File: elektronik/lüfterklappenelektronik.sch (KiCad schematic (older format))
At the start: 33 parts

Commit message: avr utils framework
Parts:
- R? (x3): value 50 -> 120
- R? (x3): value 20K -> 2K2
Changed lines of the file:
@@
 LIBS:contrib
 LIBS:valves
+LIBS:lüfterklappenelektronik-cache
 EELAYER 25 0
 EELAYER END
@@
 P 1150 1200
 F 0 "R?" H 1220 1246 50  0000 L CNN
-F 1 "50" H 1220 1155 50  0000 L CNN
+F 1 "120" H 1220 1155 50  0000 L CNN
 F 2 "" V 1080 1200 50  0000 C CNN
 F 3 "" H 1150 1200 50  0000 C CNN
@@
 P 2350 2050
 F 0 "R?" H 2420 2096 50  0000 L CNN
-F 1 "20K" H 2420 2005 50  0000 L CNN
+F 1 "2K2" H 2420 2005 50  0000 L CNN
 F 2 "" V 2280 2050 50  0000 C CNN
 F 3 "" H 2350 2050 50  0000 C CNN
@@
 P 1150 2950
 F 0 "R?" H 1220 2996 50  0000 L CNN
-F 1 "50" H 1220 2905 50  0000 L CNN
+F 1 "120" H 1220 2905 50  0000 L CNN
 F 2 "" V 1080 2950 50  0000 C CNN
 F 3 "" H 1150 2950 50  0000 C CNN
@@
 P 2350 3800
 F 0 "R?" H 2420 3846 50  0000 L CNN
-F 1 "20K" H 2420 3755 50  0000 L CNN
+F 1 "2K2" H 2420 3755 50  0000 L CNN
 F 2 "" V 2280 3800 50  0000 C CNN
 F 3 "" H 2350 3800 50  0000 C CNN
@@
 P 1150 4600
 F 0 "R?" H 1220 4646 50  0000 L CNN
-F 1 "50" H 1220 4555 50  0000 L CNN
+F 1 "120" H 1220 4555 50  0000 L CNN
 F 2 "" V 1080 4600 50  0000 C CNN
 F 3 "" H 1150 4600 50  0000 C CNN
@@
 P 2350 5450
 F 0 "R?" H 2420 5496 50  0000 L CNN
-F 1 "20K" H 2420 5405 50  0000 L CNN
+F 1 "2K2" H 2420 5405 50  0000 L CNN
 F 2 "" V 2280 5450 50  0000 C CNN
 F 3 "" H 2350 5450 50  0000 C CNN

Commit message: lot's of debugging makes things work
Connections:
- wire segments 56 -> 57
- no-connect marks 1 -> 0
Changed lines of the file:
@@
 Text Label 6750 2000 2    60   ~ 0
 PS1SS
-NoConn ~ 6450 2000
 $Comp
 L CONN_01X04 P?
@@
 Connection ~ 6550 2100
 Connection ~ 6550 1600
+Text Label 6450 2400 0    60   ~ 0
+EndstopDamper1
 Text Label 6450 2500 0    60   ~ 0
-EndstopDamper1
+EndstopDamper2
 Text Label 6450 2600 0    60   ~ 0
-EndstopDamper2
-Text Label 6450 2700 0    60   ~ 0
 EndstopDamper3
-Text Label 6450 4400 0    60   ~ 0
+Text Label 6450 3800 0    60   ~ 0
 FAN
 Text Label 6450 3400 0    60   ~ 0
@@
 Text Label 4700 800  2    60   ~ 0
 PJON
+Text Label 6450 3500 0    60   ~ 0
+PJON
+Wire Wire Line
+	6450 2000 6750 2000
+Text Label 6450 2700 0    60   ~ 0
+PS2SS
+Text Label 6450 2900 0    60   ~ 0
+PS3SS
 $EndSCHEMATC

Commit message: notes and todo
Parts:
- C?: value C -> C_SSR
- P?: value FAN_Phase -> FAN_230VAC_Phase
- R?: value R -> R_SSR
- R? (x4): value R -> 100
- U?: value S102S02 -> ZG3NC-240B
- VR?: value VR -> S7K275
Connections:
- wire segments 57 -> 58
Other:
- note added: "SSR LED pulls <=19mA per test and 40mA per datasheet\nWe _could_probably connect it directly to the Teensy via 12 Ohm R\nor maybe 47Ohm R which means 2V drop on 40mA and 0.5V drop\non 10mA so we may naturally limit the current.\nRelay LED minimum Voltage is 3V"
- moved on the sheet: P?, VR?
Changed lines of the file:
@@
 L VR VR?
 U 1 1 5741999A
-P 5750 6650
-F 0 "VR?" H 5838 6696 50  0000 L CNN
-F 1 "VR" H 5838 6605 50  0000 L CNN
-F 2 "" H 5750 6650 50  0000 C CNN
-F 3 "" H 5750 6650 50  0000 C CNN
-	1    5750 6650
+P 5850 6700
+F 0 "VR?" H 5938 6746 50  0000 L CNN
+F 1 "S7K275" H 5938 6655 50  0000 L CNN
+F 2 "" H 5850 6700 50  0000 C CNN
+F 3 "" H 5850 6700 50  0000 C CNN
+	1    5850 6700
 	1    0    0    -1
 $EndComp
@@
 P 4900 6500
 F 0 "U?" H 4900 6915 50  0000 C CNN
-F 1 "S102S02" H 4900 6824 50  0000 C CNN
+F 1 "ZG3NC-240B" H 4900 6824 50  0000 C CNN
 F 2 "SIP4_Sharp-SSR" H 4900 6733 50  0000 C CIN
 F 3 "" H 4865 6500 50  0000 L CNN
@@
 P 5450 6550
 F 0 "R?" H 5520 6596 50  0000 L CNN
-F 1 "R" H 5520 6505 50  0000 L CNN
+F 1 "R_SSR" H 5520 6505 50  0000 L CNN
 F 2 "" V 5380 6550 50  0000 C CNN
 F 3 "" H 5450 6550 50  0000 C CNN
@@
 P 5450 6850
 F 0 "C?" H 5565 6896 50  0000 L CNN
-F 1 "C" H 5565 6805 50  0000 L CNN
+F 1 "C_SSR" H 5565 6805 50  0000 L CNN
 F 2 "" H 5488 6700 50  0000 C CNN
 F 3 "" H 5450 6850 50  0000 C CNN
@@
 P 8650 1900
 F 0 "R?" V 8443 1900 50  0000 C CNN
-F 1 "R" V 8534 1900 50  0000 C CNN
+F 1 "100" V 8534 1900 50  0000 C CNN
 F 2 "" V 8580 1900 50  0000 C CNN
 F 3 "" H 8650 1900 50  0000 C CNN
@@
 P 8650 3550
 F 0 "R?" V 8443 3550 50  0000 C CNN
-F 1 "R" V 8534 3550 50  0000 C CNN
+F 1 "100" V 8534 3550 50  0000 C CNN
 F 2 "" V 8580 3550 50  0000 C CNN
 F 3 "" H 8650 3550 50  0000 C CNN
@@
 P 8650 5200
 F 0 "R?" V 8443 5200 50  0000 C CNN
-F 1 "R" V 8534 5200 50  0000 C CNN
+F 1 "100" V 8534 5200 50  0000 C CNN
 F 2 "" V 8580 5200 50  0000 C CNN
 F 3 "" H 8650 5200 50  0000 C CNN
@@
 P 4050 6950
 F 0 "R?" V 3843 6950 50  0000 C CNN
-F 1 "R" V 3934 6950 50  0000 C CNN
+F 1 "100" V 3934 6950 50  0000 C CNN
 F 2 "" V 3980 6950 50  0000 C CNN
 F 3 "" H 4050 6950 50  0000 C CNN
@@
 	3800 6950 3900 6950
 Wire Wire Line
-	5200 6400 6050 6400
+	5200 6400 6200 6400
 Connection ~ 5450 6400
-Wire Wire Line
-	5200 7000 6050 7000
-Wire Wire Line
-	5750 7000 5750 6900
 Wire Wire Line
 	5200 7000 5200 6600
@@
 L CONN_01X02 P?
 U 1 1 5741BBF0
-P 6250 6450
-F 0 "P?" H 6327 6491 50  0000 L CNN
-F 1 "FAN_Phase" H 6327 6400 50  0000 L CNN
-F 2 "" H 6250 6450 50  0000 C CNN
-F 3 "" H 6250 6450 50  0000 C CNN
-	1    6250 6450
-	1    0    0    -1
-$EndComp
-Connection ~ 5750 6400
-Wire Wire Line
-	6050 7000 6050 6500
-Connection ~ 5750 7000
+P 6400 6450
+F 0 "P?" H 6477 6491 50  0000 L CNN
+F 1 "FAN_230VAC_Phase" H 6477 6400 50  0000 L CNN
+F 2 "" H 6400 6450 50  0000 C CNN
+F 3 "" H 6400 6450 50  0000 C CNN
+	1    6400 6450
+	1    0    0    -1
+$EndComp
 $Comp
 L PHOTORESISTOR U?
@@
 Text Label 6450 2900 0    60   ~ 0
 PS3SS
+Text Notes 1400 7550 0    60   ~ 0
+SSR LED pulls <=19mA per test and 40mA per datasheet\nWe _could_probably connect it directly to the Teensy via 12 Ohm R\nor maybe 47Ohm R which means 2V drop on 40mA and 0.5V drop\non 10mA so we may naturally limit the current.\nRelay LED minimum Voltage is 3V
+Wire Wire Line
+	5850 6450 5850 6400
+Connection ~ 5850 6400
+Wire Wire Line
+	5200 7000 6200 7000
+Wire Wire Line
+	6200 7000 6200 6500
+Wire Wire Line
+	5850 6950 5850 7000
+Connection ~ 5850 7000
 $EndSCHEMATC

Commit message: update
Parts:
- removed P?: CONN_PJON, symbol CONN_01X02
- removed Q?: BC413, TO-92, symbol BC413
- added P101: CONN_01X04, symbol CONN_01X04
- gave numbers to parts that had none: 31
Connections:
- wire segments 58 -> 61
- no-connect marks 0 -> 24
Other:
- note removed: "SSR LED pulls <=19mA per test and 40mA per datasheet\nWe _could_probably connect it directly to the Teensy via 12 Ohm R\nor maybe 47Ohm R which means 2V drop on 40mA and 0.5V drop\non 10mA so we may naturally limit the current.\nRelay LED minimum Voltage is 3V"

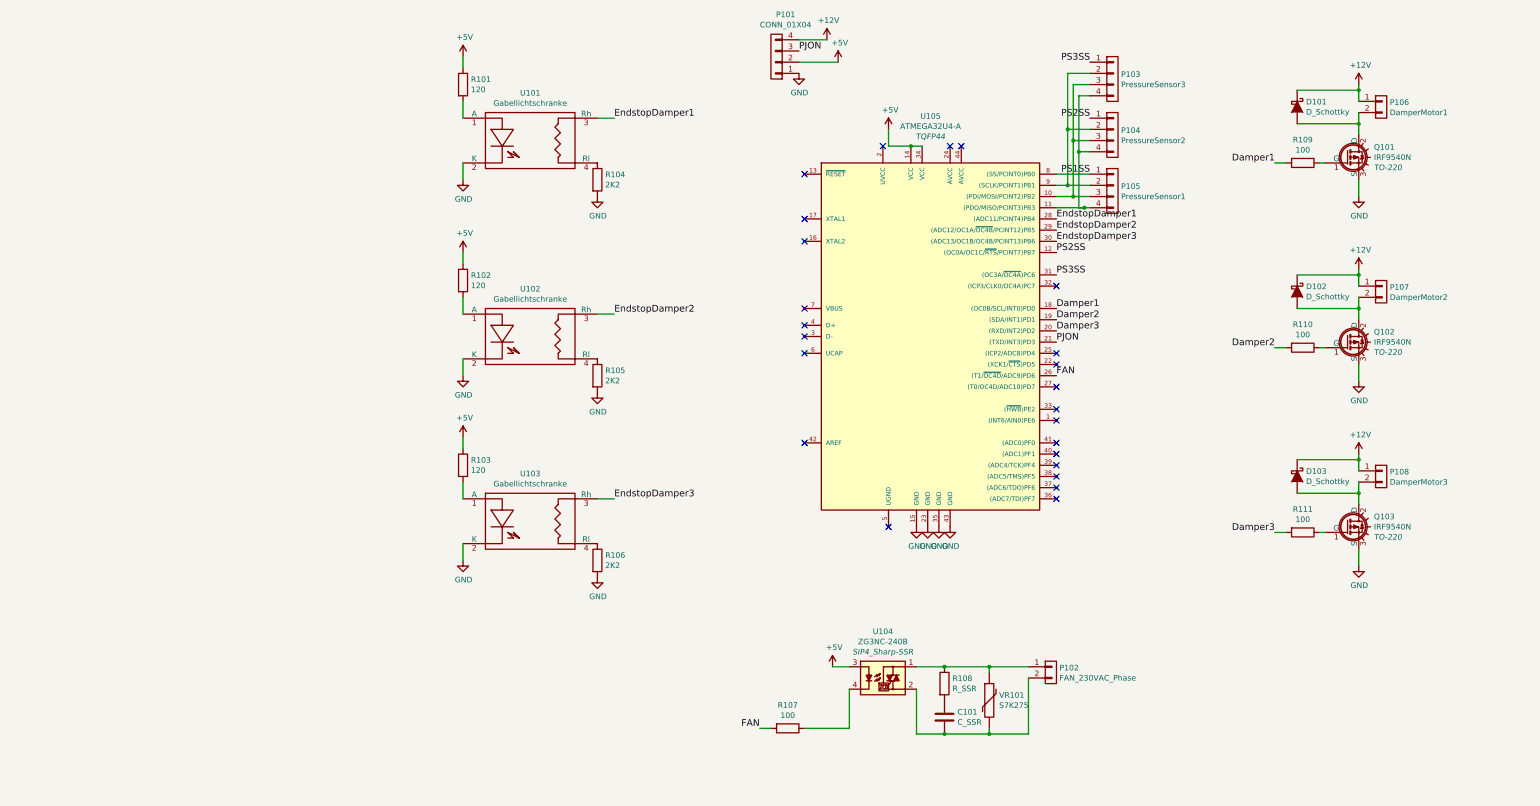
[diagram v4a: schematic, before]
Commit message: pin changes for arduinoProMicro
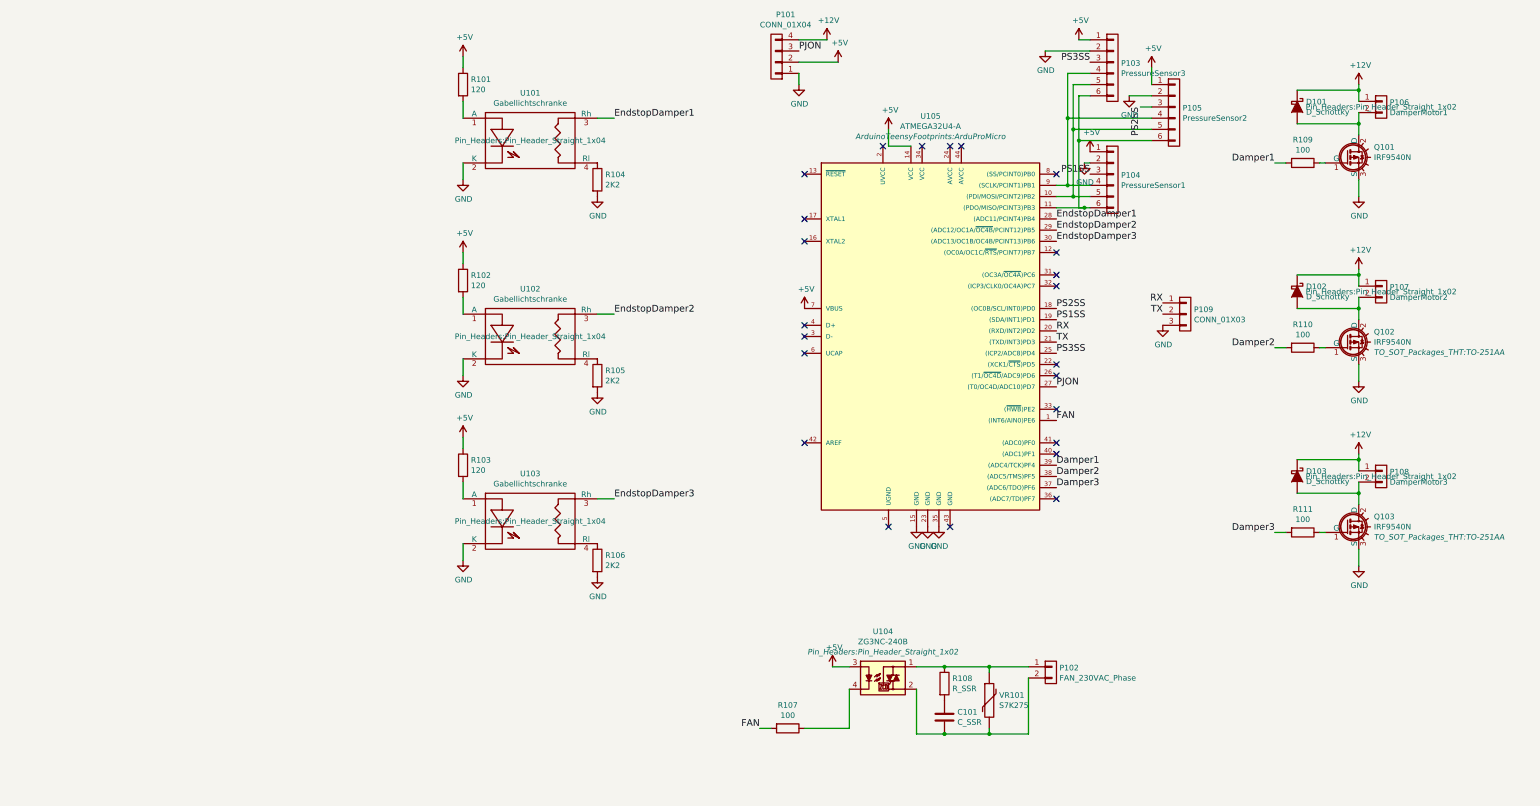
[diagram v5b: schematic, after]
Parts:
- removed P103: PressureSensor3, symbol CONN_01X04
- removed P104: PressureSensor2, symbol CONN_01X04
- removed P105: PressureSensor1, symbol CONN_01X04
- added P103: PressureSensor3, Pin_Headers:Pin_Header_Angled_1x06, symbol CONN_01X06
- added P104: PressureSensor1, Pin_Headers:Pin_Header_Angled_1x06, symbol CONN_01X06
- added P105: PressureSensor2, Pin_Headers:Pin_Header_Angled_1x06, symbol CONN_01X06
- added P109: CONN_01X03, Pin_Headers:Pin_Header_Straight_1x03, symbol CONN_01X03
- P101: footprint (none) -> Terminal_Blocks:TerminalBlock_Pheonix_MPT-2.54mm_4pol
- P106, P107, P108: footprint (none) -> Pin_Headers:Pin_Header_Straight_1x02
- Q101, Q102, Q103: footprint TO-220 -> TO_SOT_Packages_THT:TO-251AA
- R101, R102, R103, R104, R105, R106, R107, R109, R110, R111: footprint (none) -> Resistors_ThroughHole:Resistor_Horizontal_RM7mm
- U101, U102, U103: footprint (none) -> Pin_Headers:Pin_Header_Straight_1x04
- U104: footprint SIP4_Sharp-SSR -> Pin_Headers:Pin_Header_Straight_1x02
- U105: footprint TQFP44 -> ArduinoTeensyFootprints:ArduProMicro
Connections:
- net +5V: now also U105.7 (VBUS), P103.1 (P1), P104.1 (P1), P105.1 (P1); no longer U105.34 (VCC)
- net Damper1: now also U105.39 ((ADC4/TCK)PF4); no longer U105.18 ((OC0B/SCL/INT0)PD0)
- net Damper2: now also U105.38 ((ADC5/TMS)PF5); no longer U105.19 ((SDA/INT1)PD1)
- net Damper3: now also U105.37 ((ADC6/TDO)PF6); no longer U105.20 ((RXD/INT2)PD2)
- net FAN: now also U105.1 ((INT6/AIN0)PE6); no longer U105.26 ((T1/~OC4D~/ADC9)PD6)
- net GND: now also P103.2 (P2), P104.2 (P2), P105.2 (P2), P109.3 (P3); no longer U105.43 (GND)
- net PJON: now also U105.27 ((T0/OC4D/ADC10)PD7); no longer U105.21 ((TXD/INT3)PD3)
- net PS1SS: now also U105.19 ((SDA/INT1)PD1), P104.3 (P3); no longer U105.8 ((SS/PCINT0)PB0)
- net PS2SS: now also U105.18 ((OC0B/SCL/INT0)PD0), P105.3 (P3); no longer U105.12 ((OC0A/OC1C/~RTS~/PCINT7)PB7)
- net PS3SS: now also U105.25 ((ICP2/ADC8)PD4), P103.3 (P3); no longer U105.31 ((OC3A/~OC4A~)PC6)
- net at U105.10 ((PDI/MOSI/PCINT2)PB2): now also P103.5 (P5), P104.5 (P5), P105.5 (P5)
- net at U105.11 ((PDO/MISO/PCINT3)PB3): now also P103.6 (P6), P104.6 (P6), P105.6 (P6)
- net at U105.9 ((SCLK/PCINT1)PB1): now also P103.4 (P4), P104.4 (P4), P105.4 (P4)
- new net RX: P109.1 (P1), U105.20 ((RXD/INT2)PD2)
- new net TX: P109.2 (P2), U105.21 ((TXD/INT3)PD3)
- no-connect marks 24 -> 23

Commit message: some never to be used routing
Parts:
- P103, P104, P105: footprint Pin_Headers:Pin_Header_Angled_1x06 -> Pin_Headers:Pin_Header_Straight_1x06
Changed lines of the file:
@@
 F 0 "P103" H 7027 1091 50  0000 L CNN
 F 1 "PressureSensor3" H 7027 1000 50  0000 L CNN
-F 2 "Pin_Headers:Pin_Header_Angled_1x06" H 6950 1050 50  0001 C CNN
+F 2 "Pin_Headers:Pin_Header_Straight_1x06" H 6950 1050 50  0001 C CNN
 F 3 "" H 6950 1050 50  0000 C CNN
 	1    6950 1050
@@
 F 0 "P105" H 7577 1491 50  0000 L CNN
 F 1 "PressureSensor2" H 7577 1400 50  0000 L CNN
-F 2 "Pin_Headers:Pin_Header_Angled_1x06" H 7500 1450 50  0001 C CNN
+F 2 "Pin_Headers:Pin_Header_Straight_1x06" H 7500 1450 50  0001 C CNN
 F 3 "" H 7500 1450 50  0000 C CNN
 	1    7500 1450
@@
 F 0 "P104" H 7027 2091 50  0000 L CNN
 F 1 "PressureSensor1" H 7027 2000 50  0000 L CNN
-F 2 "Pin_Headers:Pin_Header_Angled_1x06" H 6950 2050 50  0001 C CNN
+F 2 "Pin_Headers:Pin_Header_Straight_1x06" H 6950 2050 50  0001 C CNN
 F 3 "" H 6950 2050 50  0000 C CNN
 	1    6950 2050

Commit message: fix symbol
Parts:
- removed Q101, Q102, Q103: IRF9540N, TO_SOT_Packages_THT:TO-251AA, symbol IRF9540N
- added Q101, Q102, Q103: IRF9540N, TO_SOT_Packages_THT:TO-251AA, symbol BUZ11
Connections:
- net GND: now also Q101.3 (S), Q102.3 (S), Q103.3 (S)
- net at R109.1: now also Q101.2 (G)
- net at D101.2 (A), P106.2 (P2): now also Q101.1 (D)
- net at R110.1: now also Q102.2 (G)
- net at D102.2 (A), P107.2 (P2): now also Q102.1 (D)
- net at R111.1: now also Q103.2 (G)
- net at D103.2 (A), P108.2 (P2): now also Q103.1 (D)
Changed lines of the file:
@@
-$EndComp
-$Comp
-L IRF9540N Q101
-U 1 1 57419A72
-P 9050 1850
-F 0 "Q101" H 9285 1941 50  0000 L CNN
-F 1 "IRF9540N" H 9285 1850 50  0000 L CNN
-F 2 "TO_SOT_Packages_THT:TO-251AA" H 9285 1759 50  0001 L CIN
-F 3 "" H 9050 1850 50  0000 L CNN
-	1    9050 1850
-	1    0    0    -1
 $EndComp
 $Comp
@@
 	8400 1900 8500 1900
 $Comp
-L IRF9540N Q102
-U 1 1 5741A878
-P 9050 3500
-F 0 "Q102" H 9285 3591 50  0000 L CNN
-F 1 "IRF9540N" H 9285 3500 50  0000 L CNN
-F 2 "TO_SOT_Packages_THT:TO-251AA" H 9285 3409 50  0000 L CIN
-F 3 "" H 9050 3500 50  0000 L CNN
-	1    9050 3500
-	1    0    0    -1
-$EndComp
-$Comp
 L D_Schottky D102
 U 1 1 5741A87E
@@
 Wire Wire Line
 	8400 3550 8500 3550
-$Comp
-L IRF9540N Q103
-U 1 1 5741AA26
-P 9050 5150
-F 0 "Q103" H 9285 5241 50  0000 L CNN
-F 1 "IRF9540N" H 9285 5150 50  0000 L CNN
-F 2 "TO_SOT_Packages_THT:TO-251AA" H 9285 5059 50  0000 L CIN
-F 3 "" H 9050 5150 50  0000 L CNN
-	1    9050 5150
-	1    0    0    -1
-$EndComp
 $Comp
 L D_Schottky D103
@@
 Wire Wire Line
 	6700 1900 6750 1900
+$Comp
+L BUZ11 Q103
+U 1 1 57544167
+P 9050 5150
+F 0 "Q103" H 9285 5241 50  0000 L CNN
+F 1 "IRF9540N" H 9285 5150 50  0000 L CNN
+F 2 "TO_SOT_Packages_THT:TO-251AA" H 9285 5059 50  0000 L CIN
+F 3 "" H 9050 5150 50  0000 L CNN
+	1    9050 5150
+	1    0    0    -1
+$EndComp
+$Comp
+L BUZ11 Q102
+U 1 1 5754473E
+P 9050 3500
+F 0 "Q102" H 9285 3591 50  0000 L CNN
+F 1 "IRF9540N" H 9285 3500 50  0000 L CNN
+F 2 "TO_SOT_Packages_THT:TO-251AA" H 9285 3409 50  0000 L CIN
+F 3 "" H 9050 3500 50  0000 L CNN
+	1    9050 3500
+	1    0    0    -1
+$EndComp
+$Comp
+L BUZ11 Q101
+U 1 1 575449DD
+P 9050 1850
+F 0 "Q101" H 9285 1941 50  0000 L CNN
+F 1 "IRF9540N" H 9285 1850 50  0000 L CNN
+F 2 "TO_SOT_Packages_THT:TO-251AA" H 9285 1759 50  0000 L CIN
+F 3 "" H 9050 1850 50  0000 L CNN
+	1    9050 1850
+	1    0    0    -1
+$EndComp
 $EndSCHEMATC

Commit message: debugging
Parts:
- removed U105: ATMEGA32U4-A, ArduinoTeensyFootprints:ArduProMicro, symbol ATMEGA32U4-A
- added A?: Arduino_Nano_v3.x, Module:Arduino_Nano, symbol MCU_Module:Arduino_Nano_v3.x
- added C?: 1µF, symbol Device:C
- added C?: 10µF, symbol Device:C
- added C? (x3): 100nF, symbol Device:C
- added C?: 1000µF, symbol Device:CP
- added D? (x3): D_Small, symbol Device:D_Small
- added R?: 0, symbol Device:R
- added U?: WeMos_mini, symbol ESP8266wemosD1:WeMos_mini
- C101: symbol C -> lüfterklappenelektronik-rescue:C
- D101, D102, D103: symbol D_Schottky -> lüfterklappenelektronik-rescue:D_Schottky
- P101: symbol CONN_01X04 -> lüfterklappenelektronik-rescue:CONN_01X04
- P102, P106, P107, P108: symbol CONN_01X02 -> lüfterklappenelektronik-rescue:CONN_01X02
- P103, P104, P105: symbol CONN_01X06 -> lüfterklappenelektronik-rescue:CONN_01X06
- P109: symbol CONN_01X03 -> lüfterklappenelektronik-rescue:CONN_01X03
- Q101, Q102, Q103: symbol BUZ11 -> lüfterklappenelektronik-rescue:BUZ11
- R101, R102, R103: value 120 -> #120; symbol R -> lüfterklappenelektronik-rescue:R
- R104, R105, R106: value 2K2 -> #2K2; symbol R -> lüfterklappenelektronik-rescue:R
- R107, R108, R109, R110, R111: symbol R -> lüfterklappenelektronik-rescue:R
- U101, U102, U103: value Gabellichtschranke -> #Gabellichtschranke; symbol PHOTORESISTOR -> lüfterklappenelektronik-rescue:PHOTORESISTOR
- U104: symbol S102S02 -> lüfterklappenelektronik-rescue:S102S02
- VR101: symbol VR -> lüfterklappenelektronik-rescue:VR
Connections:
- net labels added: MISO, MOSI, SCK
- wire segments 67 -> 94
- no-connect marks 23 -> 12
